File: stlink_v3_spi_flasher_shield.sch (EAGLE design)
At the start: 10 parts, among them CON1 STLINK_V3_HAT_BRIDGE_AND_UART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

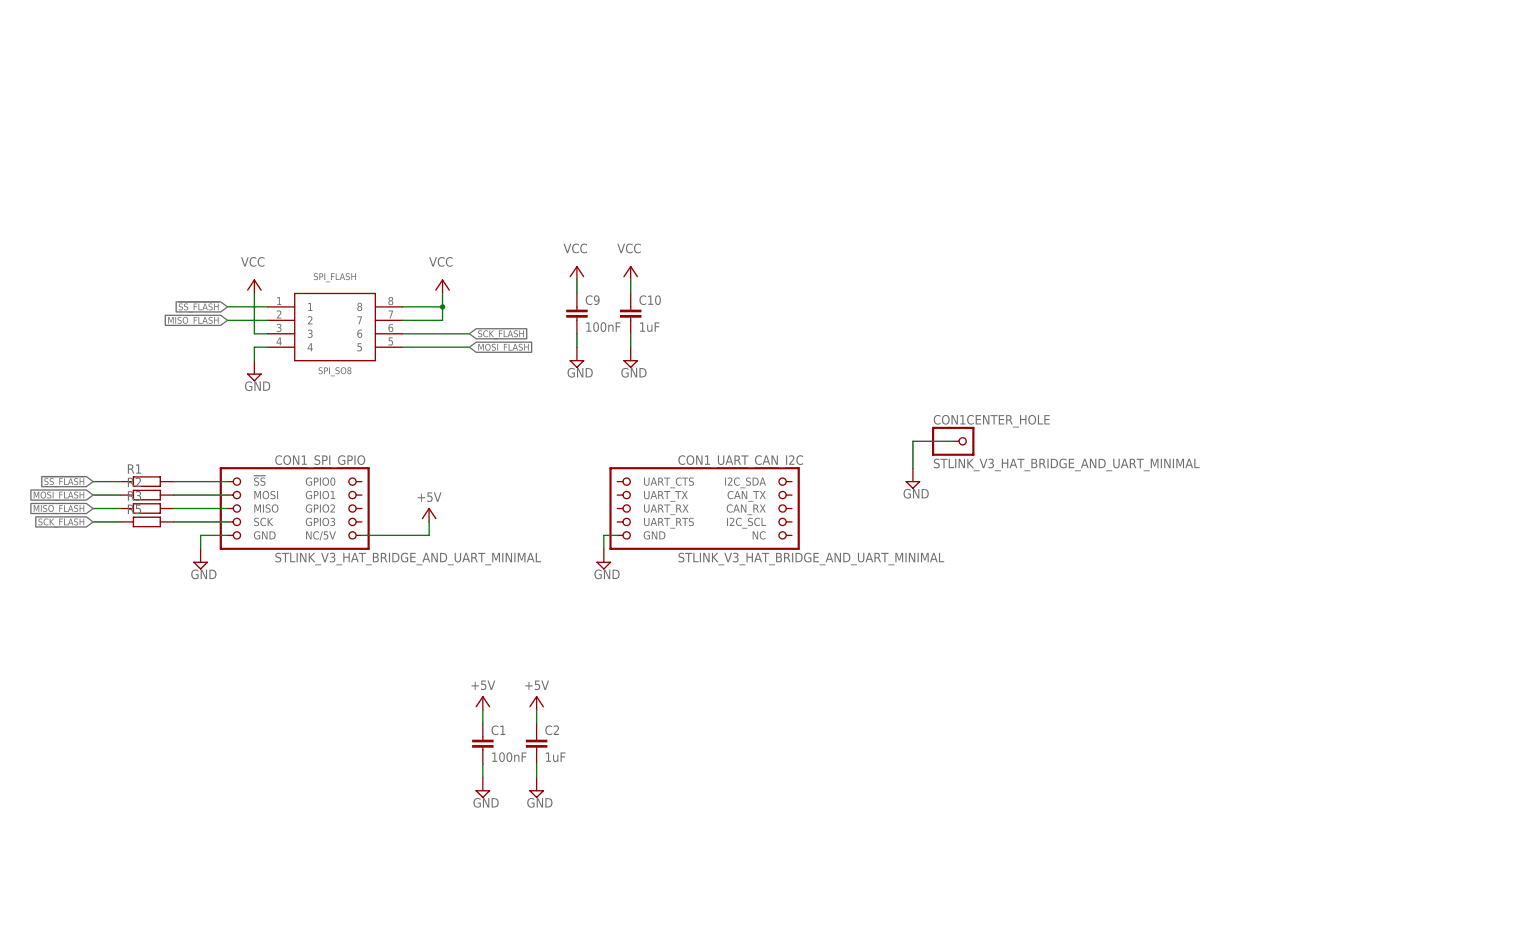
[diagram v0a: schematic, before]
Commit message: Added SPI socket
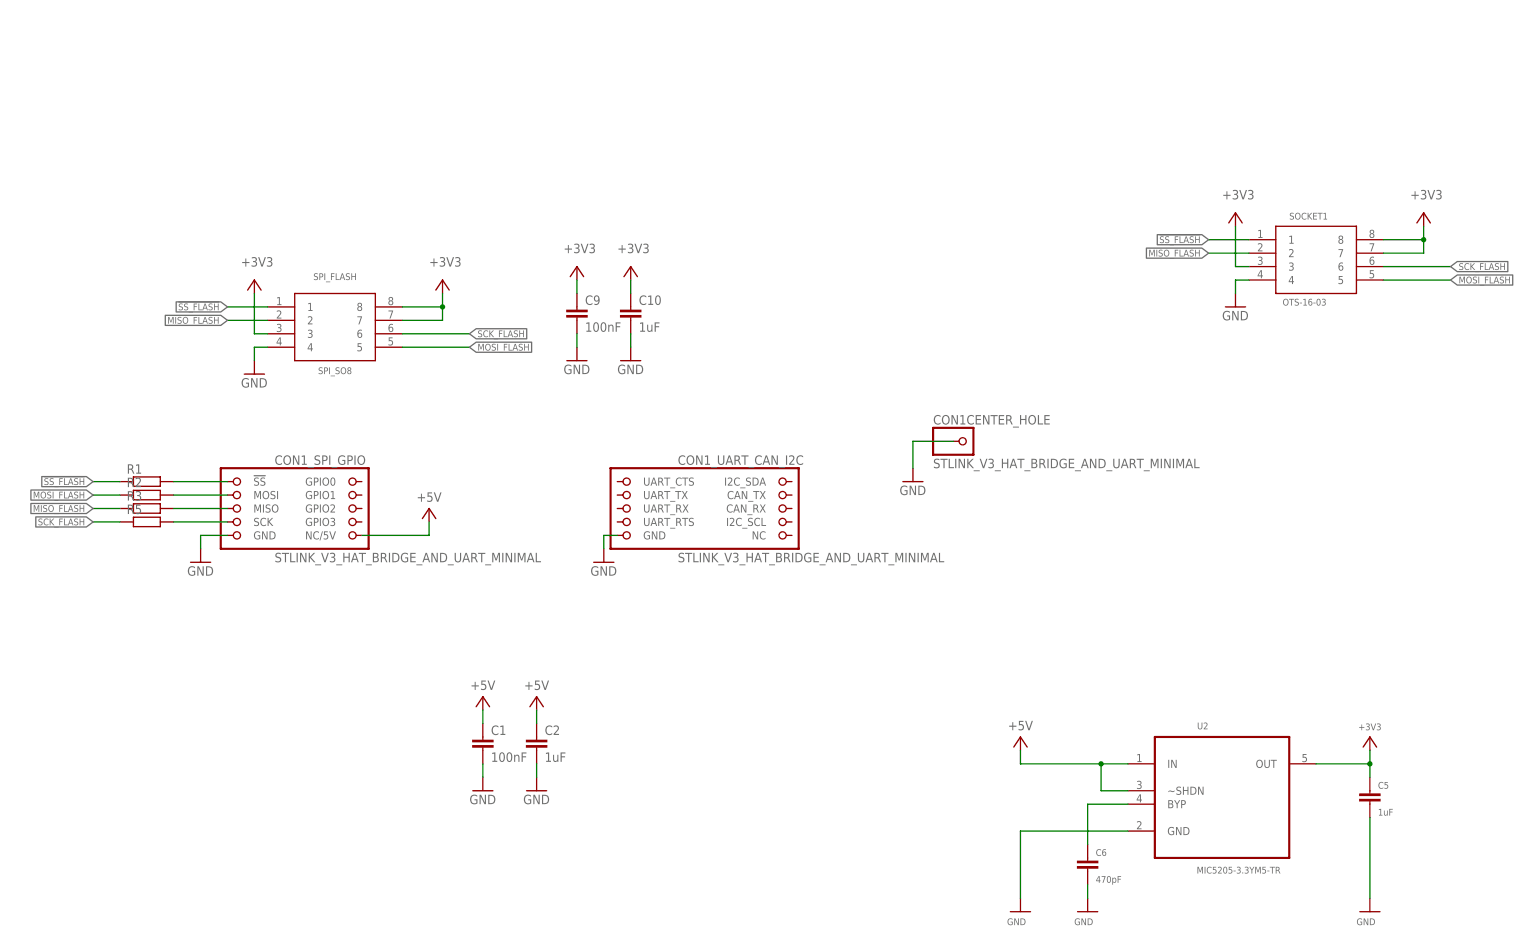
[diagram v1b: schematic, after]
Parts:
- added C5: 1uF, rcl:C-EUC0603
- added C6: 470pF, rcl:C-EUC0603
- added SOCKET1: OTS-16-03, OTS_IC_sockets:OTS-16-03
- added U2: MIC5205-3.3YM5-TR, LTC_By_element14_Batch_1:LT1761ES5-3.3TRMPBF
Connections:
- net N$1 renamed !SS_STLINK
- net N$2 renamed MOSI_STLINK
- net N$3 renamed MISO_STLINK
- net N$4 renamed SCK_STLINK
- removed net VCC: C10.1, C9.1, SPI_FLASH.3, SPI_FLASH.7, SPI_FLASH.8
- new net +3V3: C10.1, C5.1, C9.1, SOCKET1.3, SOCKET1.7, SOCKET1.8, SPI_FLASH.3, SPI_FLASH.7, SPI_FLASH.8, U2.OUT
- new net N$5: C6.1, U2.BYP
- net !SS_FLASH: now also SOCKET1.1
- net +5V: now also U2.IN, U2.~SHDN
- net GND: now also C5.2, C6.2, SOCKET1.4, U2.GND
- net MISO_FLASH: now also SOCKET1.2
- net MOSI_FLASH: now also SOCKET1.5
- net SCK_FLASH: now also SOCKET1.6

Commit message: - Added SOP16 SPI footprint - Fixup OTS socket footprint
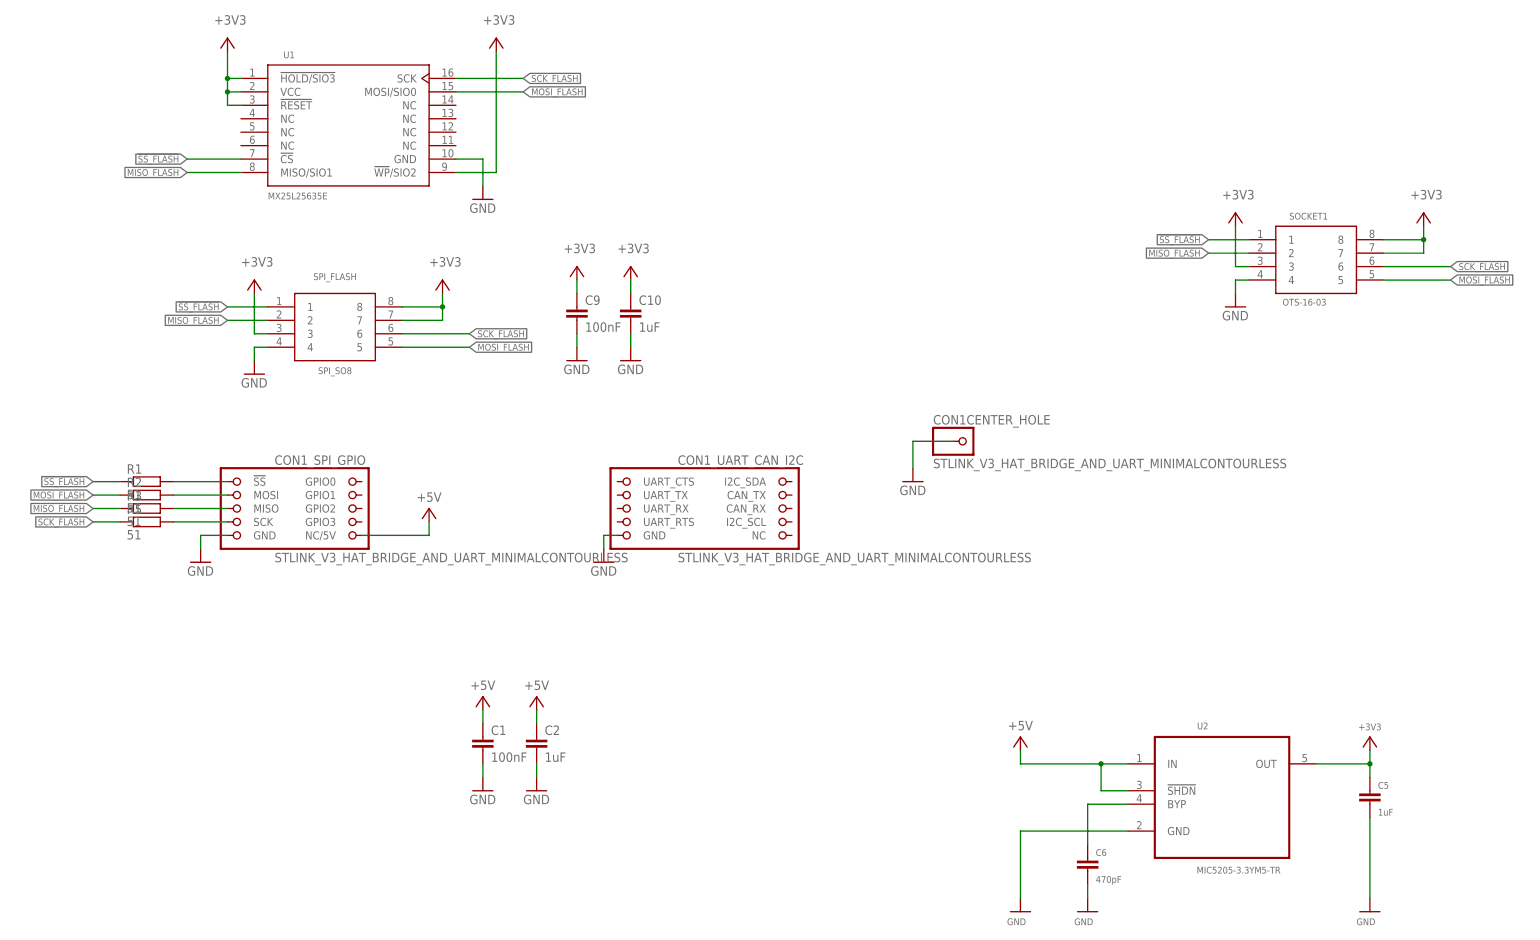
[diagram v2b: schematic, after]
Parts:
- added U1: MX25L25635E, SparkFun:MX25L25635E
- CON1: value STLINK_V3_HAT_BRIDGE_AND_UART_MINIMAL -> STLINK_V3_HAT_BRIDGE_AND_UART_MINIMALCONTOURLESS; device stlinkv3:STLINK_V3_HAT_BRIDGE_AND_UART_MINIMAL -> stlinkv3:STLINK_V3_HAT_BRIDGE_AND_UART_MINIMALCONTOURLESS
- R1, R2, R3, R5: value (none) -> 51
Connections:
- net !SS_FLASH: now also U1.!CS
- net +3V3: now also U1.!HOLD/SIO3, U1.!RESET, U1.!WP!/SIO2, U1.VCC
- net +5V: now also U2.!SHDN; no longer U2.~SHDN
- net GND: now also U1.GND
- net MISO_FLASH: now also U1.MISO/SIO1
- net MOSI_FLASH: now also U1.MOSI/SIO0
- net SCK_FLASH: now also U1.SCK
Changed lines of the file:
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@@
 <?xml version="1.0" encoding="utf-8"?>
 <!DOCTYPE eagle SYSTEM "eagle.dtd">
-<eagle version="9.6.2">
+<eagle version="9.5.2">
 <drawing>
 <settings>
@@
 <part name="P+21" library="supply1" deviceset="+3V3" device=""/>
 <part name="SPI_FLASH" library="martonmiklos" deviceset="SO8_LONG" device="" value="SPI_SO8"/>
-<part name="CON1" library="stlinkv3" deviceset="STLINK_V3_HAT_BRIDGE_AND_UART_MINIMAL" device=""/>
-<part name="R1" library="rcl" deviceset="R-EU_" device="R0603"/>
-<part name="R2" library="rcl" deviceset="R-EU_" device="R0603"/>
-<part name="R3" library="rcl" deviceset="R-EU_" device="R0603"/>
-<part name="R5" library="rcl" deviceset="R-EU_" device="R0603"/>
+<part name="CON1" library="stlinkv3" deviceset="STLINK_V3_HAT_BRIDGE_AND_UART_MINIMAL" device="CONTOURLESS" value="STLINK_V3_HAT_BRIDGE_AND_UART_MINIMALCONTOURLESS"/>
+<part name="R1" library="rcl" deviceset="R-EU_" device="R0603" value="51"/>
+<part name="R2" library="rcl" deviceset="R-EU_" device="R0603" value="51"/>
+<part name="R3" library="rcl" deviceset="R-EU_" device="R0603" value="51"/>
+<part name="R5" library="rcl" deviceset="R-EU_" device="R0603" value="51"/>
 <part name="SUPPLY1" library="supply1" deviceset="GND" device=""/>
 <part name="SUPPLY2" library="supply1" deviceset="GND" device=""/>
@@
 <part name="P+5" library="supply1" deviceset="+3V3" device=""/>
 <part name="P+6" library="supply1" deviceset="+3V3" device=""/>
+<part name="U1" library="SparkFun" deviceset="MX25L25635E" device=""/>
+<part name="P+7" library="supply1" deviceset="+3V3" device=""/>
+<part name="SUPPLY7" library="supply1" deviceset="GND" device=""/>
+<part name="P+8" library="supply1" deviceset="+3V3" device=""/>
 </parts>
 <sheets>
@@
 <attribute name="VALUE" x="218.44" y="71.12" size="1.778" layer="96"/>
 </instance>
+<instance part="U1" gate="G$1" x="53.34" y="86.36" smashed="yes">
+<attribute name="NAME" x="43.18" y="99.06" size="1.27" layer="95" rot="R180"/>
+<attribute name="VALUE" x="38.1" y="71.12" size="1.27" layer="96"/>
+</instance>
+<instance part="P+7" gate="G$1" x="30.48" y="101.6" smashed="yes">
+<attribute name="VALUE" x="27.94" y="104.14" size="1.778" layer="96"/>
+</instance>
+<instance part="SUPPLY7" gate="1" x="78.74" y="71.12" smashed="yes">
+<attribute name="VALUE" x="76.2" y="68.58" size="1.778" layer="96"/>
+</instance>
+<instance part="P+8" gate="G$1" x="81.28" y="101.6" smashed="yes">
+<attribute name="VALUE" x="78.74" y="104.14" size="1.778" layer="96"/>
+</instance>
 </instances>
 <busses>
@@
 <wire x1="220.98" y1="53.34" x2="220.98" y2="55.88" width="0.1524" layer="91"/>
 <pinref part="SOCKET1" gate="G$1" pin="4"/>
+</segment>
+<segment>
+<pinref part="U1" gate="G$1" pin="GND"/>
+<wire x1="73.66" y1="78.74" x2="78.74" y2="78.74" width="0.1524" layer="91"/>
+<pinref part="SUPPLY7" gate="1" pin="GND"/>
+<wire x1="78.74" y1="78.74" x2="78.74" y2="73.66" width="0.1524" layer="91"/>
 </segment>
 </net>
@@
 <pinref part="SOCKET1" gate="G$1" pin="3"/>
 </segment>
+<segment>
+<pinref part="U1" gate="G$1" pin="VCC"/>
+<pinref part="P+7" gate="G$1" pin="+3V3"/>
+<wire x1="33.02" y1="91.44" x2="30.48" y2="91.44" width="0.1524" layer="91"/>
+<wire x1="30.48" y1="91.44" x2="30.48" y2="93.98" width="0.1524" layer="91"/>
+<pinref part="U1" gate="G$1" pin="!HOLD/SIO3"/>
+<wire x1="30.48" y1="93.98" x2="30.48" y2="99.06" width="0.1524" layer="91"/>
+<wire x1="30.48" y1="93.98" x2="33.02" y2="93.98" width="0.1524" layer="91"/>
+<junction x="30.48" y="93.98"/>
+<pinref part="U1" gate="G$1" pin="!RESET"/>
+<wire x1="33.02" y1="88.9" x2="30.48" y2="88.9" width="0.1524" layer="91"/>
+<wire x1="30.48" y1="88.9" x2="30.48" y2="91.44" width="0.1524" layer="91"/>
+<junction x="30.48" y="91.44"/>
+</segment>
+<segment>
+<pinref part="U1" gate="G$1" pin="!WP!/SIO2"/>
+<wire x1="73.66" y1="76.2" x2="81.28" y2="76.2" width="0.1524" layer="91"/>
+<pinref part="P+8" gate="G$1" pin="+3V3"/>
+<wire x1="81.28" y1="76.2" x2="81.28" y2="99.06" width="0.1524" layer="91"/>
+</segment>
 </net>
 <net name="MOSI_FLASH" class="0">
@@
 <pinref part="SOCKET1" gate="G$1" pin="5"/>
 </segment>
+<segment>
+<pinref part="U1" gate="G$1" pin="MOSI/SIO0"/>
+<wire x1="73.66" y1="91.44" x2="86.36" y2="91.44" width="0.1524" layer="91"/>
+<label x="86.36" y="91.44" size="1.27" layer="95" font="vector" xref="yes"/>
+</segment>
 </net>
 <net name="SCK_FLASH" class="0">
@@
 <pinref part="SOCKET1" gate="G$1" pin="6"/>
 </segment>
+<segment>
+<pinref part="U1" gate="G$1" pin="SCK"/>
+<wire x1="73.66" y1="93.98" x2="86.36" y2="93.98" width="0.1524" layer="91"/>
+<label x="86.36" y="93.98" size="1.27" layer="95" font="vector" xref="yes"/>
+</segment>
 </net>
 <net name="!SS_FLASH" class="0">
@@
 <pinref part="SOCKET1" gate="G$1" pin="1"/>
 </segment>
+<segment>
+<pinref part="U1" gate="G$1" pin="!CS"/>
+<wire x1="33.02" y1="78.74" x2="22.86" y2="78.74" width="0.1524" layer="91"/>
+<label x="22.86" y="78.74" size="1.27" layer="95" font="vector" rot="R180" xref="yes"/>
+</segment>
 </net>
 <net name="!SS_STLINK" class="0">
@@
 <label x="215.9" y="60.96" size="1.27" layer="95" font="vector" rot="R180" xref="yes"/>
 <pinref part="SOCKET1" gate="G$1" pin="2"/>
+</segment>
+<segment>
+<pinref part="U1" gate="G$1" pin="MISO/SIO1"/>
+<wire x1="33.02" y1="76.2" x2="22.86" y2="76.2" width="0.1524" layer="91"/>
+<label x="22.86" y="76.2" size="1.27" layer="95" font="vector" rot="R180" xref="yes"/>
 </segment>
 </net>
@@
 <wire x1="195.58" y1="-35.56" x2="180.34" y2="-35.56" width="0.1524" layer="91"/>
 <wire x1="180.34" y1="-35.56" x2="180.34" y2="-33.02" width="0.1524" layer="91"/>
-<pinref part="U2" gate="A" pin="~SHDN"/>
+<pinref part="U2" gate="A" pin="!SHDN"/>
 <wire x1="200.66" y1="-40.64" x2="195.58" y2="-40.64" width="0.1524" layer="91"/>
 <wire x1="195.58" y1="-40.64" x2="195.58" y2="-35.56" width="0.1524" layer="91"/>
@@
 </sheet>
 </sheets>
+<errors>
+</errors>
 </schematic>
 </drawing>
